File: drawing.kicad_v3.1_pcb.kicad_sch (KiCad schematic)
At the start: 43 parts, among them IC1 DW01A-G, J1 Micro USB Chargeport, J2 Conn_01x03, J3 128x32 I2C OLED, J4 TP4056, J5 MK-12C02, J6 Conn_01x02, Q1 FS8205, U1 HT7333-SOT89, U2 ESP-12E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

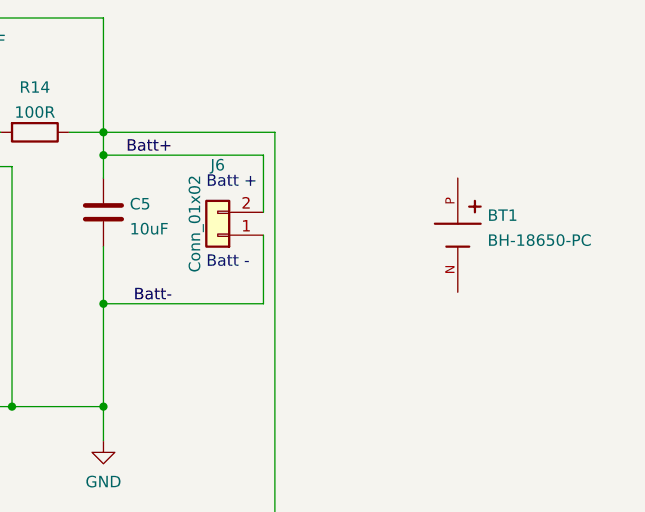
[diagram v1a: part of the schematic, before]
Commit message: Fixed HT7333 and charging circuit
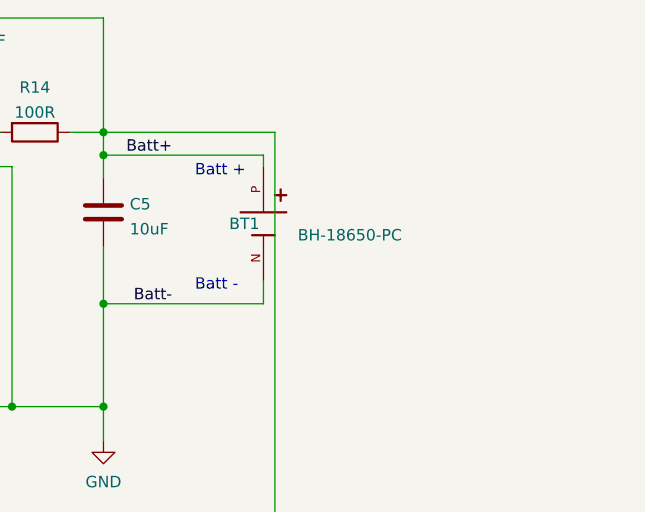
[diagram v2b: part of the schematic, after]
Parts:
- removed J6: Conn_01x02, Connector_PinSocket_2.54mm:PinSocket_1x02_P2.54mm_Vertical, symbol Connector_Generic:Conn_01x02
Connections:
- net Batt+: now also BT1.P
- net GND: now also BT1.N
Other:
- moved on the sheet: BT1
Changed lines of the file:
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@@
-    (stroke (width 0) (type default) (color 0 0 0 0))
-  )
-  (wire (pts (xy 281.94 29.21) (xy 281.94 35.56))
     (stroke (width 0) (type default) (color 0 0 0 0))
   )
@@
     (stroke (width 0) (type default) (color 0 0 0 0))
   )
+  (wire (pts (xy 281.94 29.21) (xy 281.94 30.48))
+    (stroke (width 0) (type default) (color 0 0 0 0))
+  )
   (wire (pts (xy 154.94 63.5) (xy 172.72 63.5))
     (stroke (width 0) (type default) (color 0 0 0 0))
@@
     (stroke (width 0) (type default) (color 0 0 0 0))
   )
-  (wire (pts (xy 281.94 45.72) (xy 281.94 38.1))
-    (stroke (width 0) (type default) (color 0 0 0 0))
-  )
   (wire (pts (xy 139.7 157.48) (xy 144.78 157.48))
     (stroke (width 0) (type default) (color 0 0 0 0))
@@
     (stroke (width 0) (type default) (color 0 0 0 0))
   )
+  (wire (pts (xy 281.94 43.18) (xy 281.94 45.72))
+    (stroke (width 0) (type default) (color 0 0 0 0))
+  )
   (wire (pts (xy 34.29 147.32) (xy 34.29 149.86))
     (stroke (width 0) (type default) (color 0 0 0 0))
@@
     (stroke (width 0) (type default) (color 0 0 0 0))
   )
-  (text "Batt -" (at 275.59 41.91 0)
+  (text "Batt -" (at 274.32 44.45 0)
     (effects (font (size 1.27 1.27)) (justify left bottom))
   )
-  (text "Batt +" (at 275.59 33.02 0)
+  (text "Batt +" (at 274.32 31.75 0)
     (effects (font (size 1.27 1.27)) (justify left bottom))
   )
@@
     (pin "1")
   )
-  (symbol (lib_id "BH-18650-PC:BH-18650-PC") (at 303.53 39.37 270) (unit 1)
-    (in_bom yes) (on_board yes) (fields_autoplaced)
-    (property "Reference" "BT1" (id 0) (at 306.832 35.9215 90)
-      (effects (font (size 1.27 1.27)) (justify left))
-    )
-    (property "Value" "BH-18650-PC" (id 1) (at 306.832 38.6966 90)
-      (effects (font (size 1.27 1.27)) (justify left))
-    )
-    (property "Footprint" "user-footprints:BAT_BH-18650-PC" (id 2) (at 303.53 39.37 0)
+  (symbol (lib_id "BH-18650-PC:BH-18650-PC") (at 281.94 38.1 270) (unit 1)
+    (in_bom yes) (on_board yes)
+    (property "Reference" "BT1" (id 0) (at 278.13 36.83 90)
+      (effects (font (size 1.27 1.27)) (justify left))
+    )
+    (property "Value" "BH-18650-PC" (id 1) (at 285.75 38.1 90)
+      (effects (font (size 1.27 1.27)) (justify left))
+    )
+    (property "Footprint" "user-footprints:BAT_BH-18650-PC" (id 2) (at 281.94 38.1 0)
       (effects (font (size 1.27 1.27)) (justify left bottom) hide)
     )
-    (property "Datasheet" "" (id 3) (at 303.53 39.37 0)
+    (property "Datasheet" "" (id 3) (at 281.94 38.1 0)
       (effects (font (size 1.27 1.27)) (justify left bottom) hide)
     )
-    (property "MANUFACTURER" "MPD" (id 4) (at 303.53 39.37 0)
+    (property "MANUFACTURER" "MPD" (id 4) (at 281.94 38.1 0)
       (effects (font (size 1.27 1.27)) (justify left bottom) hide)
     )
-    (property "PARTREV" "05/17/19" (id 5) (at 303.53 39.37 0)
+    (property "PARTREV" "05/17/19" (id 5) (at 281.94 38.1 0)
       (effects (font (size 1.27 1.27)) (justify left bottom) hide)
     )
-    (property "STANDARD" "Manufacturer Recommendation" (id 6) (at 303.53 39.37 0)
+    (property "STANDARD" "Manufacturer Recommendation" (id 6) (at 281.94 38.1 0)
       (effects (font (size 1.27 1.27)) (justify left bottom) hide)
     )
-    (property "MAXIMUM_PACKAGE_HEIGHT" "21.31mm" (id 7) (at 303.53 39.37 0)
+    (property "MAXIMUM_PACKAGE_HEIGHT" "21.31mm" (id 7) (at 281.94 38.1 0)
       (effects (font (size 1.27 1.27)) (justify left bottom) hide)
     )
@@
     (pin "8")
     (pin "9")
-  )
-  (symbol (lib_id "Connector_Generic:Conn_01x02") (at 276.86 38.1 180) (unit 1)
-    (in_bom yes) (on_board yes)
-    (property "Reference" "J6" (id 0) (at 276.86 30.3235 0))
-    (property "Value" "Conn_01x02" (id 1) (at 274.32 36.83 90))
-    (property "Footprint" "Connector_PinSocket_2.54mm:PinSocket_1x02_P2.54mm_Vertical" (id 2) (at 276.86 38.1 0)
-      (effects (font (size 1.27 1.27)) hide)
-    )
-    (property "Datasheet" "~" (id 3) (at 276.86 38.1 0)
-      (effects (font (size 1.27 1.27)) hide)
-    )
-    (pin "1")
-    (pin "2")
   )
   (symbol (lib_id "Device:C") (at 72.39 181.61 90) (unit 1)
@@
       (reference "J5") (unit 1) (value "MK-12C02") (footprint "user-footprints:MK12C02")
     )
-    (path "/bf117efd-79a6-444a-b75c-3b8af1ec3b81"
-      (reference "J6") (unit 1) (value "Conn_01x02") (footprint "Connector_PinSocket_2.54mm:PinSocket_1x02_P2.54mm_Vertical")
-    )
     (path "/83d18630-c7e8-4218-9c71-f36bb281f280"
